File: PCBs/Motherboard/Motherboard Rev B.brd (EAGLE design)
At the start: 95.9 x 90.2 mm, 54 parts, among them J1 MOLEX_504050-0491, Q1 32kHZ, U1 Value

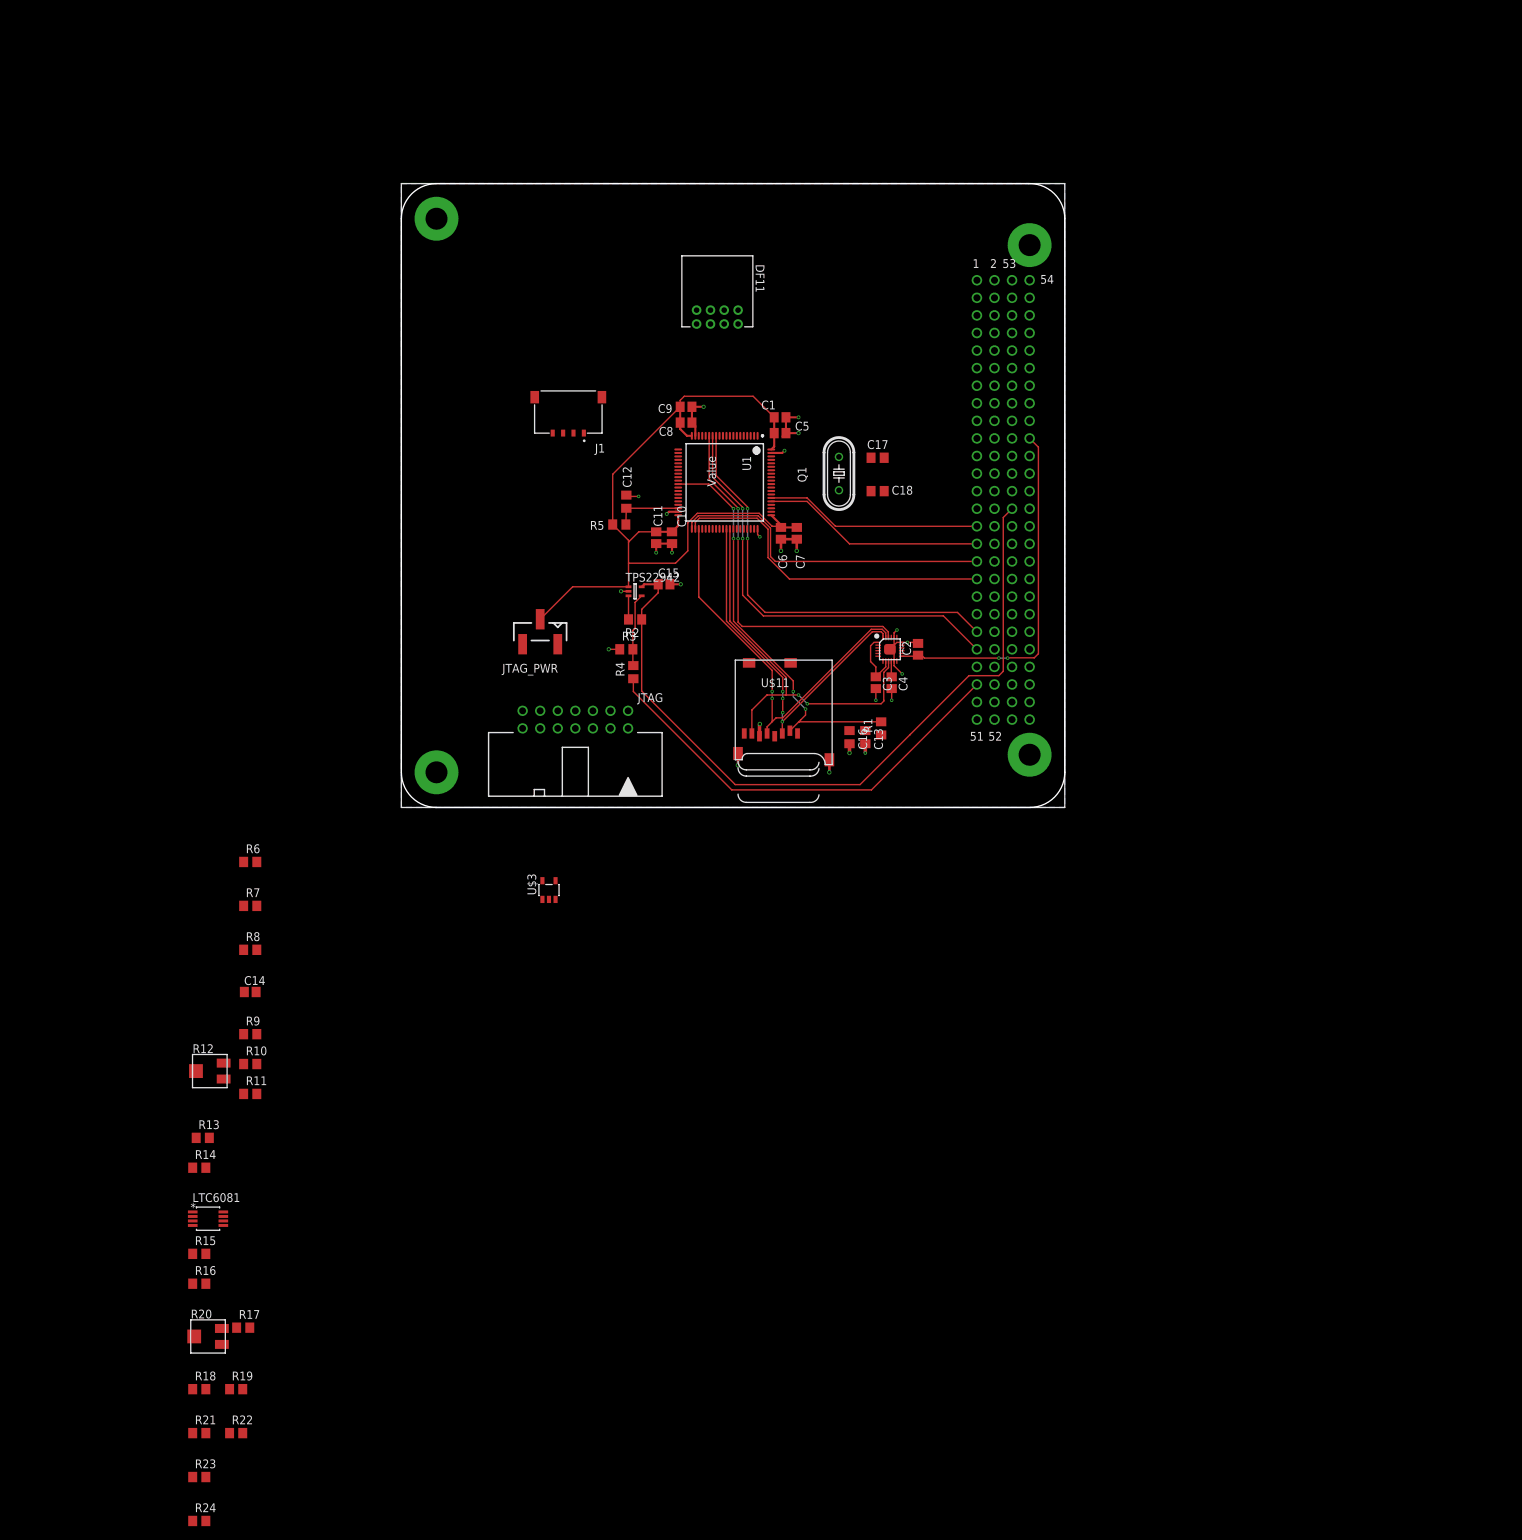
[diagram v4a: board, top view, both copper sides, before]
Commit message: Split I2C and SPI buses
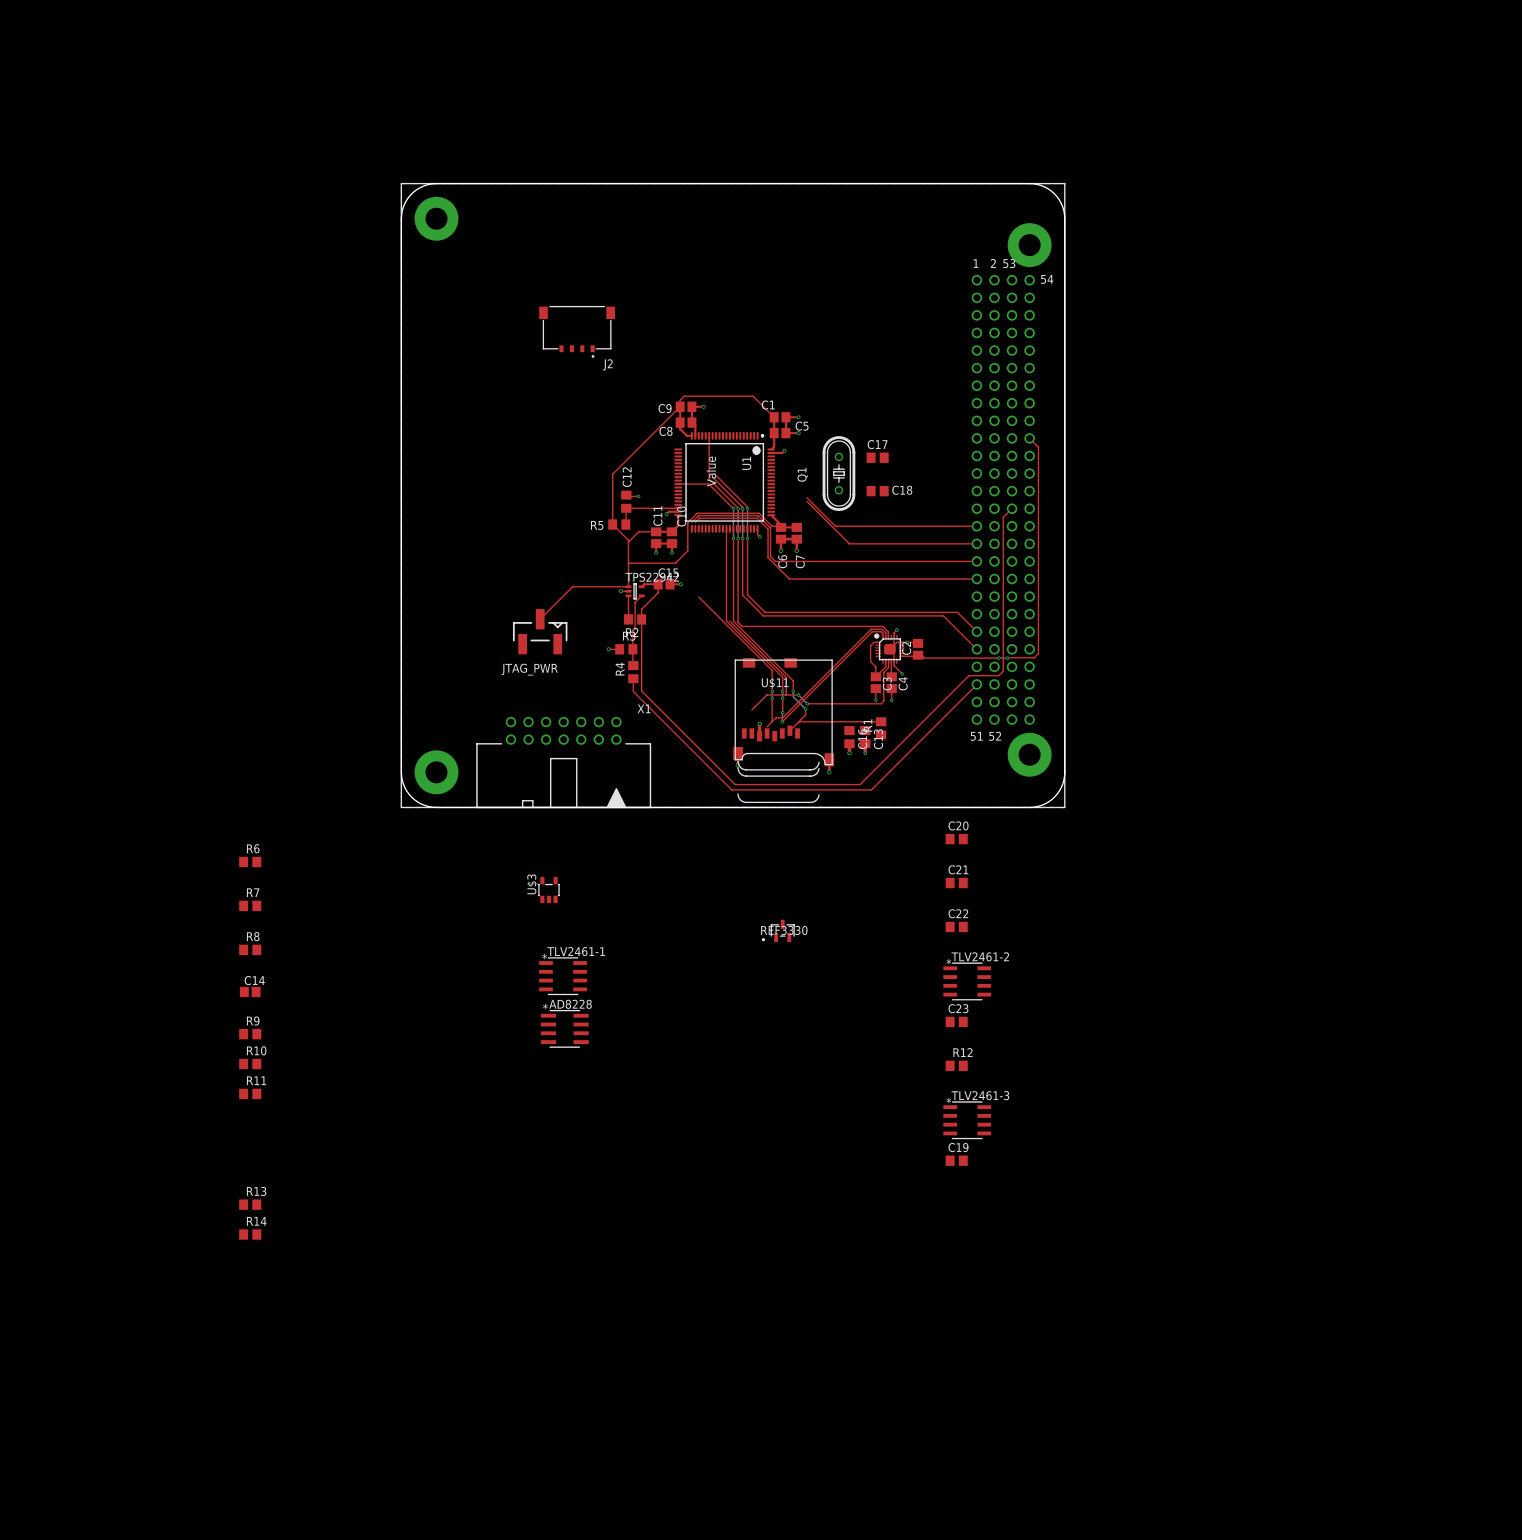
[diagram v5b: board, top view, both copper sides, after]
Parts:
- removed DF11: DF11-8DP-2DS(52), DF11:CON8_2X4_RF_DF11
- removed J1: MOLEX_504050-0491, Molex 504050-0491:MOLEX_5040500491
- removed JTAG: 2514-5, con-3m:PAK100/2500-5-14
- removed LTC6081: LTC6081HMS8PBF, LTC6081:MSOP-8_MS
- removed R15, R16, R23, R24: 330k, resistor:R0805
- removed R17, R18, R19: 350, resistor:R0805
- removed R20: 50, Bourns 3224J:3224J
- removed R21, R22: 10k, resistor:R0805
- added AD8228: AD8228BRZ, AD8228:R_8
- added C19, C20, C21, C22, C23: 0.1uF, resistor:C0805
- added J2: MOLEX_504050-0491, Molex 504050-0491:MOLEX_5040500491
- added REF3330: REF3330_DBZ_3, REF3330:DBZ3
- added TLV2461-1, TLV2461-2, TLV2461-3: TLV2461A_D_8, TLV2461:D8
- added X1: 2514-5, con-3m:PAK100/2500-5-14
- C17, C18: value 10pF -> 6pF
- R10, R11: value 350 -> 10k
- R12: value 50 -> 100; device Bourns 3224J:3224J -> resistor:R0805
- R13, R14: value 10k -> 0
- moved R12 108.0 mm to (80.3, -37.3)
- moved R14 12.1 mm to (-21.8, -61.7)
- moved R13 11.8 mm to (-21.8, -57.4)
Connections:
- removed net MISO: U$11.7, U$2.9, U1.52
- removed net MOSI: U$11.3, U$2.24, U1.51
- removed net N$12: LTC6081.5, R21.2, R23.2
- removed net N$13: LTC6081.6, R22.2, R24.2
- removed net SCL: J1.2, U$1.43, U1.14
- removed net SCLK: U$11.5, U$2.23, U1.43
- removed net SDA: J1.3, U$1.41, U1.13
- removed net STR1: LTC6081.1, R16.1, U1.5
- removed net STR1_L1: DF11.1, R12.2
- removed net STR1_L2: DF11.2, R9.2
- removed net STR1_L3: DF11.3, R14.1
- removed net STR2: LTC6081.7, R24.1, U1.6
- removed net STR2_L1: DF11.4, R20.2
- removed net STR2_L2: DF11.5, R17.2
- removed net STR2_L3: DF11.6, R22.1
- removed net TMP_L1: DF11.7
- removed net TMP_L2: DF11.8
- new net 3V: J2.1, J2.3, R11.2, TLV2461-1.2, TLV2461-1.6
- new net 3V_REF: REF3330.2, TLV2461-1.3
- new net CLK_IMU: U$2.23, U1.55
- new net CLK_SD: U$11.5, U1.43
- new net JTAG_RXD: R13.1, U1.35
- new net JTAG_TXD: R14.1, U1.36
- new net MISO_IMU: U$2.9, U1.54
- new net MISO_SD: U$11.7, U1.52
- new net MOSI_IMU: U$2.24, U1.53
- new net MOSI_SD: U$11.3, U1.51
- new net SCL_ANT: U$1.39, U1.70
- new net SCL_EPS: U$1.43, U1.14
- new net SDA_ANT: U$1.37, U1.69
- new net SDA_EPS: U$1.41, U1.13
- new net SHIELD: J2.SH1, J2.SH2
- new net STRAIN_OUT: AD8228.1, AD8228.7, R10.2, R11.1, TLV2461-2.3, U1.5
- new net STRN: AD8228.4, J2.4, R9.2
- new net TEMP: J2.2, R12.2, TLV2461-3.3
- new net TEMP_OUT: TLV2461-3.2, TLV2461-3.6, U1.6
- net 3V3: now also AD8228.8, C21.1
- net EXT_RXD: now also U1.8; no longer JTAG.14, U1.36
- net EXT_TXD: now also U1.9; no longer JTAG.12, U1.35
- net GND: now also AD8228.5, C19.2, C20.2, C21.2, C22.2, C23.2, R12.1, REF3330.3, TLV2461-1.4, TLV2461-2.4, X1.9; no longer J1.4, J1.SH1, J1.SH2, JTAG.9, LTC6081.4, R15.1, R17.1, R18.1, R23.1
- net LITHIUM_RX: now also U1.65; no longer U1.66
- net LITHIUM_TX: now also U1.66; no longer U1.65
- net N$10: now also TLV2461-3.4; no longer LTC6081.2, R14.2, R16.2
- net N$11: now also R13.2, X1.12; no longer R18.2, R19.1, R21.1
- net N$8: now also R14.2, X1.14; no longer R10.2, R11.1, R13.1
- net N$9: now also AD8228.6, TLV2461-2.2, TLV2461-2.6; no longer LTC6081.3, R13.2, R15.2
- net PINAVL1_RX: now also U1.41; no longer U1.42
- net PINAVL1_TX: now also U1.42; no longer U1.41
- net SBWTCK: now also X1.7; no longer JTAG.7
- net SBWTDIO: now also X1.1; no longer JTAG.1
- net SW10: now also C19.1, C20.1, C22.1, C23.1, REF3330.1, TLV2461-1.7, TLV2461-2.7, TLV2461-3.7; no longer LTC6081.8, R11.2, R12.1, R19.2, R20.1
- net SW5: no longer J1.1
- net VCC_TARGET: now also X1.4; no longer JTAG.4
- net VCC_TOOL: now also X1.2; no longer JTAG.2
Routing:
- net SCL: track 61.9 -> 0.00 mm, vias 2 -> 0
- net SDA: track 60.2 -> 0.00 mm, vias 2 -> 0
- net MISO: track 57.5 -> 0.00 mm, vias 2 -> 0
- net SCLK: track 57.1 -> 0.00 mm, vias 2 -> 0
- net SCL_EPS: track 0.00 -> 55.9 mm, vias 0 -> 2
- net SDA_EPS: track 0.00 -> 54.5 mm, vias 0 -> 2
- net MOSI: track 53.6 -> 0.00 mm, vias 4 -> 0
- net MOSI_IMU: track 0.00 -> 51.9 mm, vias 0 -> 4
- net CLK_IMU: track 0.00 -> 46.3 mm, vias 0 -> 2
- net MISO_IMU: track 0.00 -> 40.8 mm, vias 0 -> 2
- net LITHIUM_RX: track 31.4 -> 26.2 mm
- net LITHIUM_TX: track 32.3 -> 27.1 mm
- net PINAVL1_TX: track 47.7 -> 46.7 mm
- net PINAVL1_RX: track 47.9 -> 47.0 mm

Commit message: Add SD card detect to 7.2
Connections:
- new net SD_DETECT: U$11.CD1, U1.25
- net GND: now also U$11.CD2
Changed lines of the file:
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@@
 <contactref element="C19" pad="2"/>
 <contactref element="X1" pad="9"/>
-<wire x1="81.214" y1="-51.054" x2="20.922" y2="12.345" width="0" layer="19" extent="1-1"/>
-<wire x1="79.314" y1="-37.338" x2="81.214" y2="-51.054" width="0" layer="19" extent="1-1"/>
-<wire x1="81.214" y1="-30.988" x2="79.314" y2="-37.338" width="0" layer="19" extent="1-1"/>
-<wire x1="79.3242" y1="-27.051" x2="81.214" y2="-30.988" width="0" layer="19" extent="1-1"/>
-<wire x1="81.214" y1="-17.272" x2="79.3242" y2="-27.051" width="0" layer="19" extent="1-1"/>
-<wire x1="81.214" y1="-10.922" x2="81.214" y2="-17.272" width="0" layer="19" extent="1-1"/>
-<wire x1="81.214" y1="-4.572" x2="81.214" y2="-10.922" width="0" layer="19" extent="1-1"/>
-<wire x1="25.9842" y1="-33.909" x2="81.214" y2="-4.572" width="0" layer="19" extent="1-1"/>
-<wire x1="20.9042" y1="-26.289" x2="25.9842" y2="-33.909" width="0" layer="19" extent="1-1"/>
-<wire x1="-22.794" y1="-37.084" x2="20.9042" y2="-26.289" width="0" layer="19" extent="1-1"/>
-<wire x1="-22.794" y1="-32.766" x2="-22.794" y2="-37.084" width="0" layer="19" extent="1-1"/>
-<wire x1="-20.994" y1="-26.67" x2="-22.794" y2="-32.766" width="0" layer="19" extent="1-1"/>
-<wire x1="-22.794" y1="-7.874" x2="-20.994" y2="-26.67" width="0" layer="19" extent="1-1"/>
-<wire x1="55.118" y1="-16.89735" x2="25.9842" y2="-33.909" width="0" layer="19" extent="1-1"/>
-<wire x1="21.336" y1="-13.288" x2="-20.994" y2="-26.67" width="0" layer="19" extent="1-1"/>
-<wire x1="48.641" y1="6.096" x2="21.336" y2="-13.288" width="0" layer="19" extent="1-1"/>
-<wire x1="51.76" y1="10.296" x2="48.66" y2="7.796" width="0" layer="19" extent="1-1"/>
+<contactref element="U$11" pad="CD2"/>
+<wire x1="88.265" y1="40.64" x2="88.265" y2="50.8" width="0" layer="19" extent="1-1"/>
+<wire x1="90.805" y1="40.64" x2="88.265" y2="40.64" width="0" layer="19" extent="1-1"/>
+<wire x1="90.805" y1="38.1" x2="90.805" y2="40.64" width="0" layer="19" extent="1-1"/>
+<wire x1="69.784" y1="50.546" x2="88.265" y2="50.8" width="0" layer="19" extent="1-1"/>
+<wire x1="69.784" y1="45.72" x2="69.784" y2="50.546" width="0" layer="19" extent="1-1"/>
+<wire x1="57.15" y1="38.774" x2="69.784" y2="45.72" width="0" layer="19" extent="1-1"/>
+<wire x1="51.816" y1="39.116" x2="54.864" y2="38.774" width="0" layer="19" extent="1-1"/>
+<wire x1="40.011" y1="42.74" x2="51.486" y2="40.265" width="0" layer="19" extent="1-1"/>
+<wire x1="39.116" y1="38.139" x2="38.354" y2="42.418" width="0" layer="19" extent="1-1"/>
+<wire x1="38.823" y1="32.258" x2="39.116" y2="36.83" width="0" layer="19" extent="1-1"/>
+<wire x1="34.29" y1="44.958" x2="38.354" y2="42.418" width="0" layer="19" extent="1-1"/>
+<wire x1="32.832003125" y1="31.242" x2="38.823" y2="32.258" width="0" layer="19" extent="1-1"/>
+<wire x1="31.562" y1="22.86" x2="31.75" y2="31.242" width="0" layer="19" extent="1-1"/>
+<wire x1="42.486" y1="53.715" x2="40.011" y2="42.74" width="0" layer="19" extent="1-1"/>
+<wire x1="20.922" y1="12.345" x2="29.972" y2="22.86" width="0" layer="19" extent="1-1"/>
+<wire x1="56.26" y1="20.896" x2="57.15" y2="37.084" width="0" layer="19" extent="1-1"/>
+<wire x1="51.816" y1="12.065" x2="56.26" y2="20.896" width="0" layer="19" extent="1-1"/>
+<wire x1="48.66" y1="7.796" x2="51.76" y2="10.296" width="0" layer="19" extent="1-1"/>
 <wire x1="61.86" y1="6.896" x2="51.76" y2="10.296" width="0" layer="19" extent="1-1"/>
 <wire x1="64.77" y1="7.874" x2="61.86" y2="6.896" width="0" layer="19" extent="1-1"/>
@@
 <wire x1="88.265" y1="17.78" x2="74.676" y2="23.71" width="0" layer="19" extent="1-1"/>
 <wire x1="90.805" y1="17.78" x2="88.265" y2="17.78" width="0" layer="19" extent="1-1"/>
-<wire x1="57.15" y1="37.084" x2="71.212" y2="25.238" width="0" layer="19" extent="1-1"/>
-<wire x1="51.816" y1="39.116" x2="54.864" y2="38.774" width="0" layer="19" extent="1-1"/>
-<wire x1="40.011" y1="42.74" x2="51.486" y2="40.265" width="0" layer="19" extent="1-1"/>
-<wire x1="39.116" y1="38.139" x2="38.354" y2="42.418" width="0" layer="19" extent="1-1"/>
-<wire x1="38.823" y1="32.258" x2="39.116" y2="36.83" width="0" layer="19" extent="1-1"/>
-<wire x1="34.29" y1="44.958" x2="38.354" y2="42.418" width="0" layer="19" extent="1-1"/>
-<wire x1="32.832003125" y1="31.242" x2="38.823" y2="32.258" width="0" layer="19" extent="1-1"/>
-<wire x1="31.562" y1="22.86" x2="31.75" y2="31.242" width="0" layer="19" extent="1-1"/>
-<wire x1="42.486" y1="53.715" x2="40.011" y2="42.74" width="0" layer="19" extent="1-1"/>
-<wire x1="69.784" y1="45.72" x2="57.15" y2="38.774" width="0" layer="19" extent="1-1"/>
-<wire x1="69.784" y1="50.546" x2="69.784" y2="45.72" width="0" layer="19" extent="1-1"/>
-<wire x1="88.265" y1="50.8" x2="69.784" y2="50.546" width="0" layer="19" extent="1-1"/>
-<wire x1="88.265" y1="40.64" x2="88.265" y2="50.8" width="0" layer="19" extent="1-1"/>
-<wire x1="90.805" y1="40.64" x2="88.265" y2="40.64" width="0" layer="19" extent="1-1"/>
-<wire x1="90.805" y1="38.1" x2="90.805" y2="40.64" width="0" layer="19" extent="1-1"/>
+<wire x1="81.214" y1="-4.572" x2="67.056" y2="7.874" width="0" layer="19" extent="1-1"/>
+<wire x1="81.214" y1="-10.922" x2="81.214" y2="-4.572" width="0" layer="19" extent="1-1"/>
+<wire x1="81.214" y1="-17.272" x2="81.214" y2="-10.922" width="0" layer="19" extent="1-1"/>
+<wire x1="79.3242" y1="-27.051" x2="81.214" y2="-17.272" width="0" layer="19" extent="1-1"/>
+<wire x1="81.214" y1="-30.988" x2="79.3242" y2="-27.051" width="0" layer="19" extent="1-1"/>
+<wire x1="79.314" y1="-37.338" x2="81.214" y2="-30.988" width="0" layer="19" extent="1-1"/>
+<wire x1="81.214" y1="-51.054" x2="79.314" y2="-37.338" width="0" layer="19" extent="1-1"/>
+<wire x1="55.118" y1="-16.89735" x2="61.849" y2="5.08" width="0" layer="19" extent="1-1"/>
+<wire x1="21.336" y1="-13.288" x2="20.922" y2="12.345" width="0" layer="19" extent="1-1"/>
+<wire x1="20.9042" y1="-26.289" x2="21.336" y2="-13.288" width="0" layer="19" extent="1-1"/>
+<wire x1="25.9842" y1="-33.909" x2="20.9042" y2="-26.289" width="0" layer="19" extent="1-1"/>
+<wire x1="-20.994" y1="-26.67" x2="20.9042" y2="-26.289" width="0" layer="19" extent="1-1"/>
+<wire x1="-22.794" y1="-32.766" x2="-20.994" y2="-26.67" width="0" layer="19" extent="1-1"/>
+<wire x1="-22.794" y1="-37.084" x2="-22.794" y2="-32.766" width="0" layer="19" extent="1-1"/>
+<wire x1="-22.794" y1="-7.874" x2="-20.994" y2="-26.67" width="0" layer="19" extent="1-1"/>
 </signal>
 <signal name="3V3">
@@
 <wire x1="18.382" y1="9.805" x2="-20.894" y2="-57.404" width="0" layer="19" extent="1-1"/>
 </signal>
+<signal name="SD_DETECT">
+<contactref element="U$11" pad="CD1"/>
+<contactref element="U1" pad="25"/>
+<wire x1="50.26" y1="20.896" x2="40.011" y2="49.74" width="0" layer="19" extent="1-1"/>
+</signal>
 </signals>

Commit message: Replace SD connector with a model hand-solderable
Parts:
- removed U$11: MICROSD, adafruit:MICROSD
- added SD_CONN: 502702-0891, Molex SD - 502702:502702
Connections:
- net 3V3_SD: now also SD_CONN.4; no longer U$11.4
- net CLK_SD: now also SD_CONN.5; no longer U$11.5
- net CS_SD: now also SD_CONN.2; no longer U$11.2
- net GND: now also SD_CONN.6, SD_CONN.GND; no longer U$11.6, U$11.CD2, U$11.MT1, U$11.MT2
- net MISO_SD: now also SD_CONN.7; no longer U$11.7
- net MOSI_SD: now also SD_CONN.3; no longer U$11.3
- net SD_DETECT: now also SD_CONN.DET; no longer U$11.CD1
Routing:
- net MOSI_IMU: track 51.9 -> 0.00 mm, vias 4 -> 0
- net CLK_IMU: track 46.3 -> 0.00 mm, vias 2 -> 0
- net MISO_IMU: track 40.8 -> 6.08 mm, vias 2 -> 0
- net CS_SD: track 58.7 -> 37.9 mm, vias 4 -> 2
- net SCL_EPS: track 55.9 -> 61.9 mm
- net SDA_EPS: track 54.5 -> 60.2 mm
- net GND: track 48.4 -> 43.1 mm, vias 21 -> 18
- net SW10: track 60.9 -> 58.0 mm, vias 2 -> 0
- net LI_OA_RESET: track 63.7 -> 65.9 mm
- net 3V3: track 107.7 -> 109.4 mm
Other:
- outline, holes or cut-outs redrawn
